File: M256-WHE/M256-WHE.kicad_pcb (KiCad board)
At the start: 2 copper layers, 301.8 x 97 mm, 253 parts, among them J1 JST_SH, J2 TC2030, SW1 TS-1187A-B-A-B, SW2 TS-1187A-B-A-B, U1 USBLC6-2SC6, U2 TLV75733PDBV, U3 XC6206P332MR-G, U4 STM32F446RET6, Y1 X322516MLB4SI

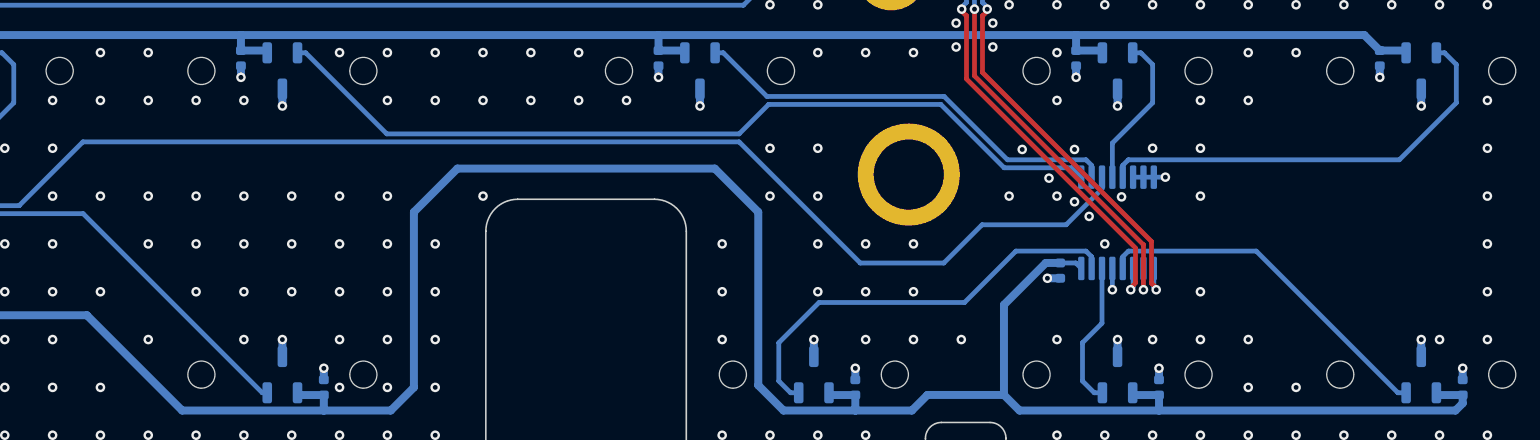
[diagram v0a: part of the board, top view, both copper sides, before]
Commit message: :art: move logo on the PCB
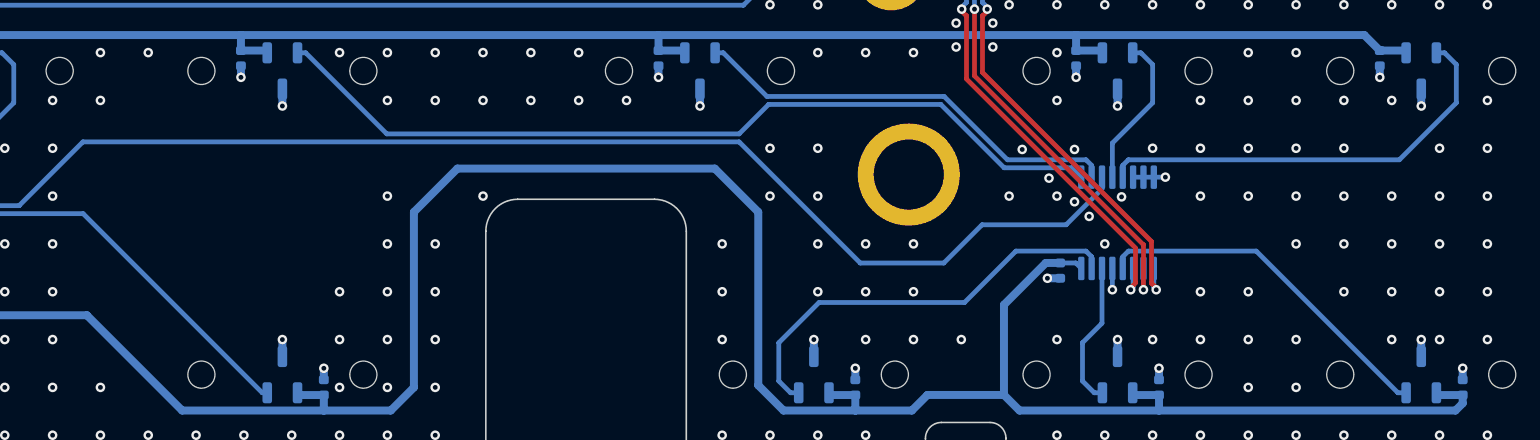
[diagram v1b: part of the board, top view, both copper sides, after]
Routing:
- net GND: vias 2129 -> 2131

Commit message: :sparkles: change OH49E-S Hall sensors to DRV5055A3
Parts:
- HE1, HE10, HE11, HE12, HE13, HE14, HE15, HE16, HE17, HE18, HE19, HE2, HE20, HE21, HE22, HE23, HE24, HE25, HE26, HE27, HE28, HE29, HE3, HE30, HE31, HE32, HE33, HE34, HE35, HE36, HE37, HE38, HE39, HE4, HE40, HE41, HE42, HE43, HE44, HE45, HE46, HE47, HE48, HE49, HE5, HE50, HE51, HE52, HE53, HE54, HE55, HE56, HE57, HE58, HE59, HE6, HE60, HE61, HE62, HE63, HE64, HE65, HE66, HE67, HE68, HE7, HE8, HE9: value OH49E-S -> DRV5055A3QDBZR

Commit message: :art: update via stitch spacing
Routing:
- net GND: vias 2131 -> 1344

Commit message: :art: move around some traces
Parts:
- moved C91 0.45 mm to (98.6, 79.8)
- moved C89 0.20 mm to (104.4, 79.2)
- moved C90 0.20 mm to (102.0, 79.2)
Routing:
- net +3.3V: track 248.3 -> 229.5 mm, vias 9 -> 8
- net +3.3VA: track 1738.0 -> 1741.9 mm
- net VBUS: track 3.50 -> 0.14 mm
- net NRST: track 97.0 -> 94.9 mm
- net MUX_OUT_2: track 118.5 -> 120.4 mm
- net MUX_OUT_4: track 104.0 -> 105.8 mm
- net MUX_OUT_6: track 75.4 -> 76.0 mm
- net GND: track 181.9 -> 181.8 mm, vias 1344 -> 1503
- added copper zone on B.Cu, net VBUS
